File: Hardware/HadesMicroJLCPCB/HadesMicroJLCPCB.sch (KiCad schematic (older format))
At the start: 84 parts, among them IC1 MPRLS0015PA0000SA, U1 AP2112K-3.3, U2 PCA9685PW, U3 CAT24C256, U4 USBLC6-2SC6, U5 74AHC1GU04GW,125, U6 CH340E

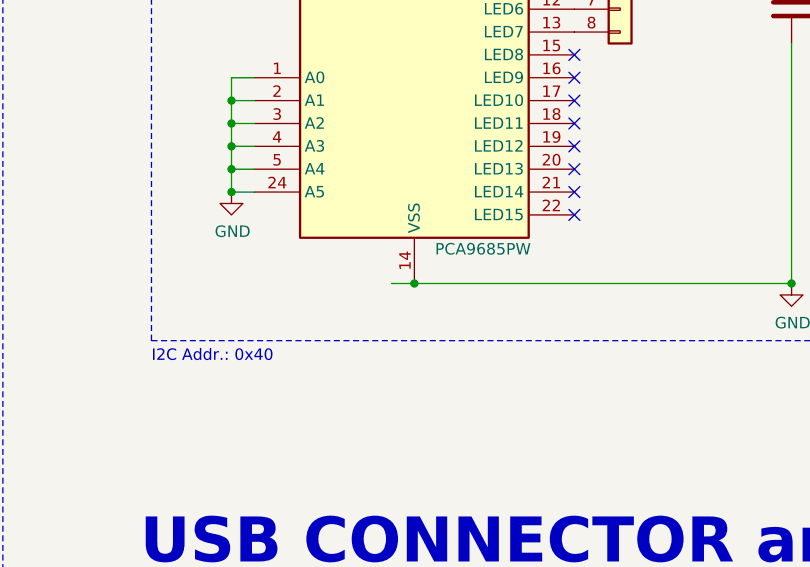
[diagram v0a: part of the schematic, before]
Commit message: Updated Hades Micro (JLCPCB) silkscreen.
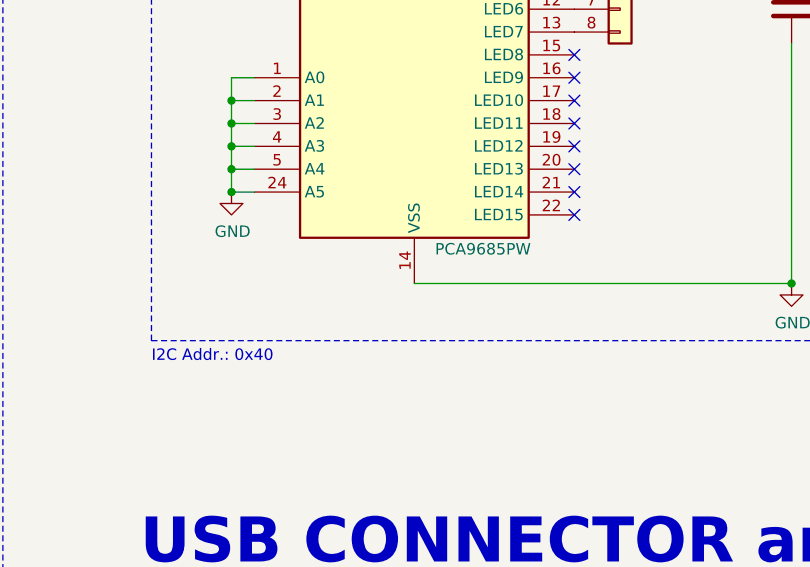
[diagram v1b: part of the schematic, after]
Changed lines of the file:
@@
 Title "Hades Micro"
 Date "2019-12-05"
-Rev ""
-Comp ""
+Rev "v0.1"
+Comp "Philip Salmony"
 Comment1 ""
 Comment2 ""
@@
 $EndComp
 Wire Wire Line
-	11000 3150 11100 3150
-Connection ~ 11100 3150
-Wire Wire Line
 	11100 3150 12750 3150

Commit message: NAVC debug software real-time plotting.
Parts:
- SERVO1: footprint Connector_Molex:Molex_PicoBlade_53048-0210_1x02_P1.25mm_Horizontal -> TerminalBlock_Phoenix:TerminalBlock_Phoenix_PT-1,5-2-3.5-H_1x02_P3.50mm_Horizontal
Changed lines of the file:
@@
 F 0 "SERVO1" H 14730 1242 50  0000 L CNN
 F 1 "TrmnlBlck" H 14730 1151 50  0000 L CNN
-F 2 "Connector_Molex:Molex_PicoBlade_53048-0210_1x02_P1.25mm_Horizontal" H 14650 1250 50  0001 C CNN
+F 2 "TerminalBlock_Phoenix:TerminalBlock_Phoenix_PT-1,5-2-3.5-H_1x02_P3.50mm_Horizontal" H 14650 1250 50  0001 C CNN
 F 3 "~" H 14650 1250 50  0001 C CNN
 	1    14650 1250
